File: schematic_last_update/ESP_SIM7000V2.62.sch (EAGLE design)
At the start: 72 parts, among them J1 U.FL-R-SMT(01), J2 U.FL-R-SMT(01), J3 78646-3001, Q1 SI2305CDS, Q2 BSS138, Q3 SI2305CDS, Q4 BSS138, Q5 SI2305CDS, Q6 BSS138, Q7 BSS138, Q8 BSS138, Q9 BSS138, U1 ESP-WROOM-03, U3 TXB0104D, U4 MIC5239S, X1 S2B-PH-K-S, X2 B2B-PH-K-S

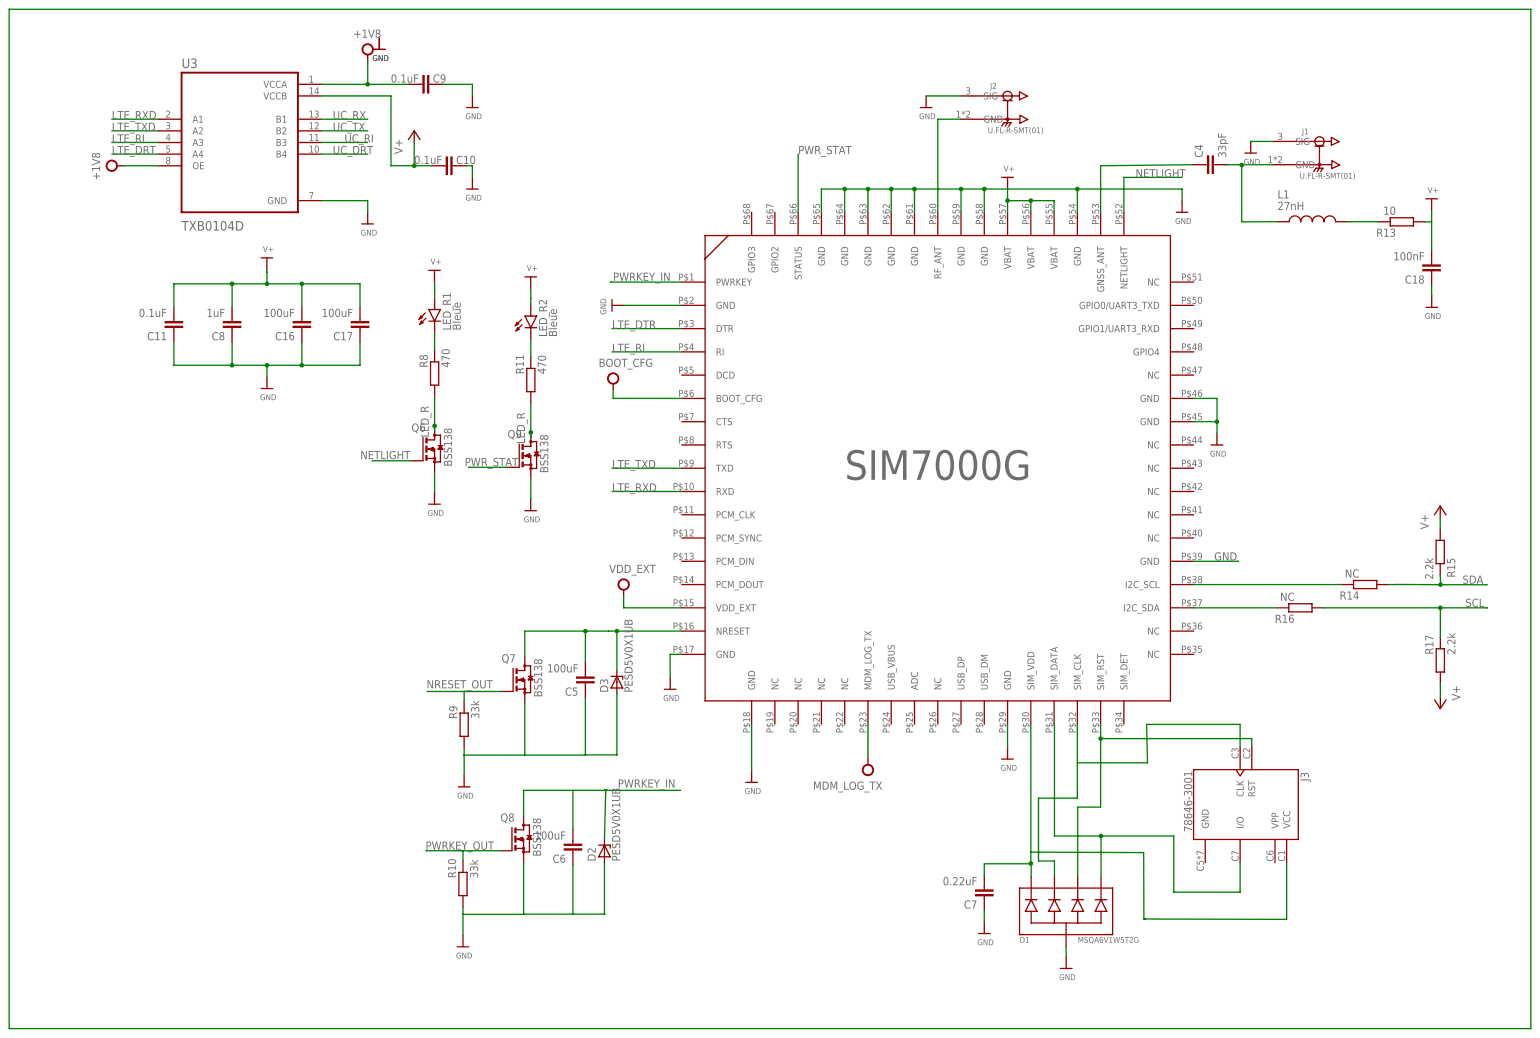
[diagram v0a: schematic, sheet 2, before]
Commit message: Correction schematic et ajout de TXB0108PWR
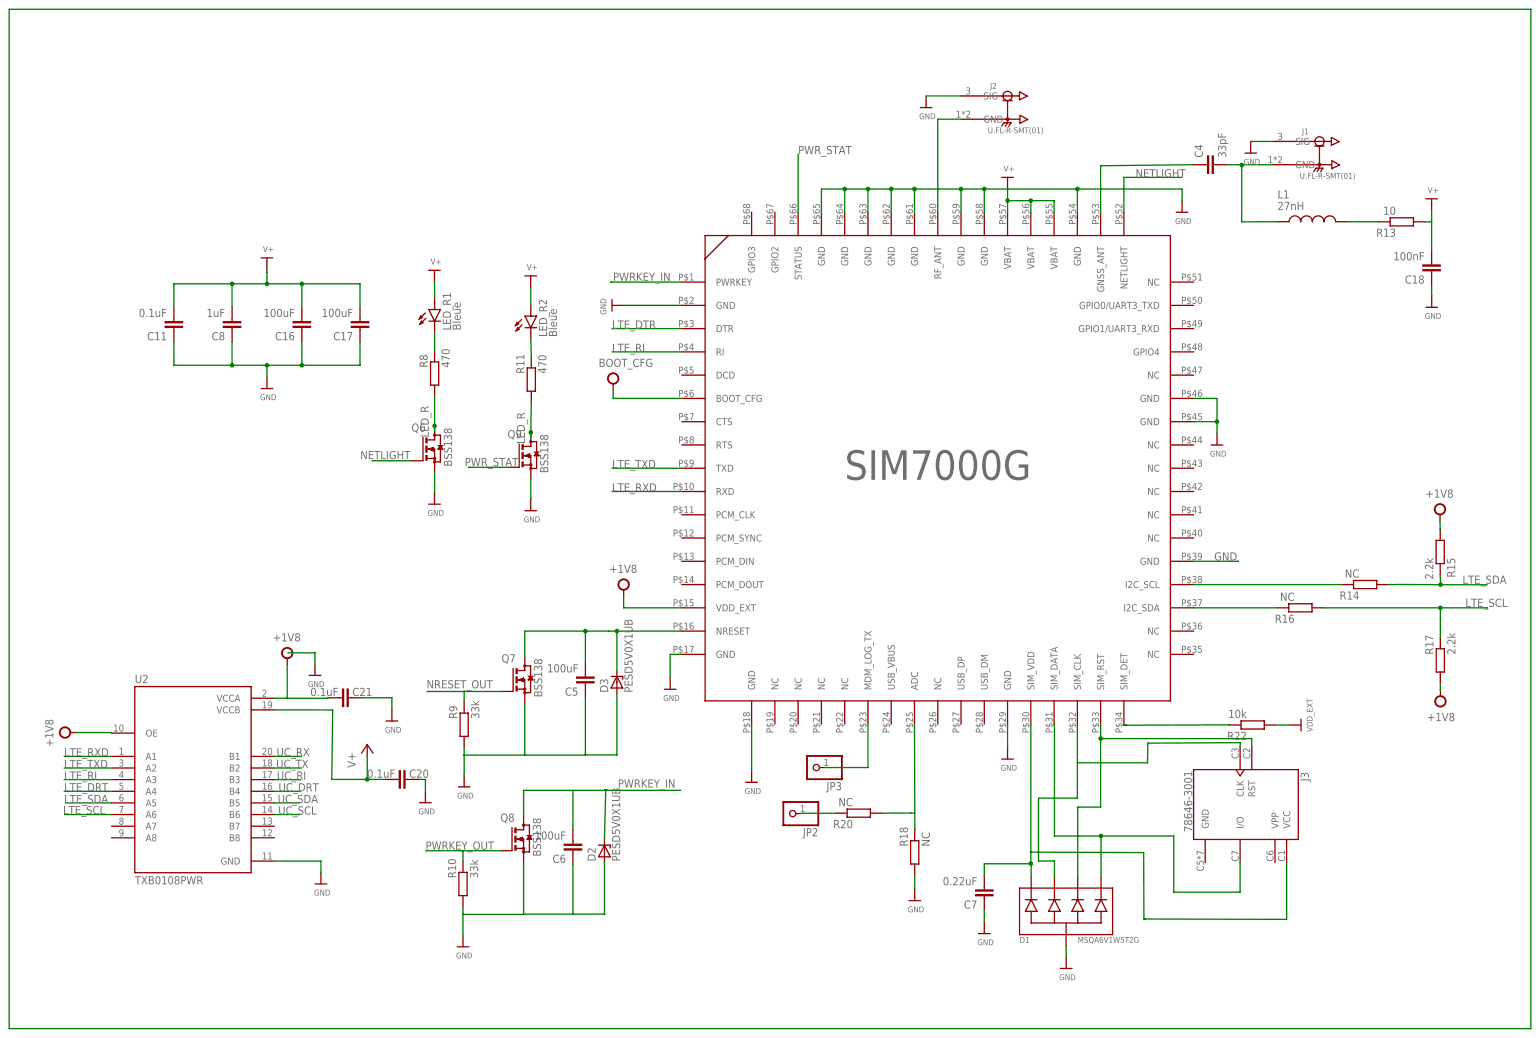
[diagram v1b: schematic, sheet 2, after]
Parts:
- removed C10, C9: 0.1uF, eagle-ltspice:CC1210
- removed U3: TXB0104D, TXB0104D:TXB0104D
- added C20, C21: 0.1uF, eagle-ltspice:CC1210
- added JP2, JP3: (no value), pinhead:PINHD-1X1
- added R18, R20: NC, eagle-ltspice:RR1206
- added R22: 10k, eagle-ltspice:RR1206
- added U2: TXB0108PWR, TXB0108PWR:TXB0108PWR
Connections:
- removed net LTE_DRT: U3.A4
- removed net SCL: R16.1, R17.2, U1.IO22
- removed net SDA: R14.1, R15.2, U1.IO21
- new net LTE_SCL: R16.1, R17.2, U2.A6
- new net LTE_SDA: R14.1, R15.2, U2.A5
- new net N$42: R18.2, U$1.ADC
- new net N$43: R22.2
- new net N$44: U$1.SIM_DET
- new net N$45: JP3.1, U$1.MDM_LOG_TX
- new net UC_SCL: U1.IO22, U2.B6
- new net UC_SDA: U1.IO21, U2.B5
- new net VDD: Q3.D
- net +1V8: now also C21.2, R15.1, R17.1, U2.OE, U2.VCCA; no longer C9.2, U$1.MDM_LOG_TX, U3.OE, U3.VCCA
- net +3V3: no longer R15.1
- net +5V: now also C20.2, U2.VCCB; no longer C10.2, U3.VCCB
- net GND: now also C20.1, C21.1, LED_R2.A, R18.1, R22.1, U2.GND; no longer C10.1, C9.1, U3.GND
- net LTE_RI: no longer U3.A3
- net LTE_RXD: no longer U3.A1
- net LTE_TXD: no longer U3.A2
- net N$34: now also R20.1; no longer LED_R2.A
- net UC_DRT: now also U2.B4; no longer U3.B4
- net UC_RI: now also U2.B3; no longer U3.B3
- net UC_RX: now also U2.B1; no longer U3.B1
- net UC_TX: now also U2.B2; no longer U3.B2
- net V+: no longer Q3.D, R17.1
